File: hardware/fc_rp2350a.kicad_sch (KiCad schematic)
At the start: 49 parts, among them Q1 AP1606, Q2 AP1606, U1 TS2306A 240GF MSM 9_C2976675, U2 RP2354A, X1 XTM25012000JT00351001

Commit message: Circuit: B3 bulk caps and ESP32-C3FH4, LDO caps, BMI270 aux pins, BOOTSEL 1k, unused pads
CIRCUIT_REVIEW B3, S2, S4, S5 and decision D9; LAYOUT_REVIEW 5.3 (pure
clean-up). Values and parts from hardware/KiCad-Library/PARTS-USED.md.

- B3: the 16 +BATT bulk caps had value "C" and no part. C90-C103 (0805)
  4.7uF 50V X5R CL21A475KBQNNNE (C98192, already C18/C19); C105/C106 (1206)
  4.7uF 50V X7R TCC1206X7R475K500HT (C380366, OpenESC).
- D9/B3: U22 is ESP32-C3FH4 (C2858491, in-package flash), as its NC SPI pins
  require; its in-package-flash pads 19, 21-24 deleted per instance (20 was
  already gone). L4 MPN MLZ2012M150WT000 (TDK, SX1281 reference BOM, LCSC not
  in the catalogue); D9 MPN/manufacturer/LCSC from the catalogue.
- S2, LP5912 windows (CIN > 0.5 uF effective, COUT 0.7-10 uF): U7 COUT C28
  22uF -> 1uF CL05A105KA5NQNC; U6 COUT C27 22uF -> 4.7uF CL05A475MP5NRNC;
  U7 CIN C26 100nF -> 1uF GRM033R61A105ME44D in the existing 0201 (an 0402
  does not fit beside U7 without moving parts; ~0.5 uF effective at 4.6 V,
  so it is marginal until U7 moves to the Core in R2, decision S1).
- S4: BMI270 U8 ASDx/ASCx (pins 2/3) were on GND, which the datasheet
  forbids; now +3.3V (VDDIO), valid for the LSM6DSV16X option too.
  Schematic: the GND drop replaced by a +3.3V symbol. Core: pads 2/3 and the
  via between them re-netted, 0.15 mm In3 stub to the In3 +3.3V pour.
- S5: BOOTSEL resistor R7 10k -> 1k (0201WMF1001TEE, C270365): 10k with the
  32k minimum pull-up gave 0.79 V against VIL 0.8 V.
- LAYOUT_REVIEW 5.3, pads on no net with nothing attached: U13/U15/U17/U19
  (AT32F421) 3, 8, 9, 12, 23, 24, 26-28; U14/U16/U18/U20 (NSG2065Q) NC 5, 7,
  8, 21; U7 NC 2; U21 6 (XTB, TCXO), 9, 10 (DIO2/3); Core U2 55-59 (QSPI,
  in-package flash). 60 pads in all; U8 kept for joint symmetry. AT32
  firmware must keep the dropped pins as outputs or pulled.
- Footprint values and fields synced from the schematic for the changed refs.

Deferred: RX LED D9 to +4v5 (S10). +4v5 copper is 1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
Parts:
- R7: value 10k -> 1k; LCSC C106225 -> C270365; MPN RC0201FR-0710KL -> 0201WMF1001TEE; Manufacturer YAGEO -> UNI-ROYAL
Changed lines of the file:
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@@
 			)
 		)
-		(property "Value" "10k"
+		(property "Value" "1k"
 			(at 259.08 212.09 90)
 			(show_name no)
@@
 			)
 		)
-		(property "LCSC" "C106225"
+		(property "LCSC" "C270365"
 			(at 259.08 207.01 0)
 			(hide yes)
@@
 			)
 		)
-		(property "MPN" "RC0201FR-0710KL"
+		(property "MPN" "0201WMF1001TEE"
 			(at 71.12 46.99 0)
 			(hide yes)
@@
 			)
 		)
-		(property "Manufacturer" "YAGEO"
+		(property "Manufacturer" "UNI-ROYAL"
 			(at 71.12 46.99 0)
 			(hide yes)

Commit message: Owner rules: no component silk, pad labels and values, no wordmark text, MPN + maker on every BOM line
The owner rules adopted in PLAN.md (pcb-agent-commons, 2026-10-06), applied
where they are local edits:

- No component silkscreen. J91's reference was the only visible one (Core
  B.Silkscreen, under the LGA) and is hidden. Footprint silk graphics removed
  per instance: Base 234, Core 72. Kept: connector outlines and pin-1 marks
  (USB1, U12 SH-6, Card1, JP1) and the LGA pin-1 marks (J90, J91). Base
  lib_footprint_mismatch warnings 31 -> 40 as a result.
- Solder-pad labels: Core J53 (GND) had none, now "gnd" in the style of J52's
  label. The SH-6 per-pin labels ("10v gnd T0", "R0 gnd R1") become the port
  name "DJI" (connectors: name and pin-1 mark only). Core J48-J51 have no room:
  0.5 mm to J44 above, 0.93 mm to the board edge below. CIRCUIT_REVIEW 8.3
  moves them off the LGA in R2, so their labels go with that move.
- Pad values: all 40 solder-pad symbols said "5V". Each now carries its
  function (5V, GND, LED, BUZ+/BUZ-, 10V, 4V5, CAM, VTX, SCL, SDA, TX0/RX0,
  TX1/RX1, PIO_TX0/PIO_RX0; off-board J19 ADC2, J22 GND, J46/J47 NC).
- No "Drone" text: the "OpenDrone" wordmark on Core F.Silkscreen (9 filled
  polygons in two groups) is removed; a TODO for the incutec wordmark from the
  brand repo sits on User.Comments (not fabricated). No other such text on any
  copper, mask or silk layer of either board.
- BOM: lines missing manufacturer or MPN 41 -> 1. MPNs come from
  PARTS-USED.md by LCSC number. Manufacturers come from the catalogue symbol,
  this design's spelling for the same MPN family, or the committed datasheet
  (NSIC, Sofng, Jiangsu Changjing, Hirose). Still open: Rsense2
  ASR-S-3-0.2F (C695806), whose manufacturer nothing in the catalogue states.
  U24 (board outline) and TP9 (BOOT solder pad) are not parts: excluded from
  BOM and position files.
- 0201 default / minimal capacitance: respected in the circuit commit (C26
  stays 0201; no belt-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
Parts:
- R14: MPN (none) -> RTT012401FTH; Manufacturer (none) -> RALEC
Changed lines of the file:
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@@
 			)
 		)
-		(property "MPN" ""
+		(property "MPN" "RTT012401FTH"
 			(at 171.45 138.43 0)
 			(hide yes)
@@
 			)
 		)
-		(property "Manufacturer" ""
+		(property "Manufacturer" "RALEC"
 			(at 171.45 138.43 0)
 			(hide yes)

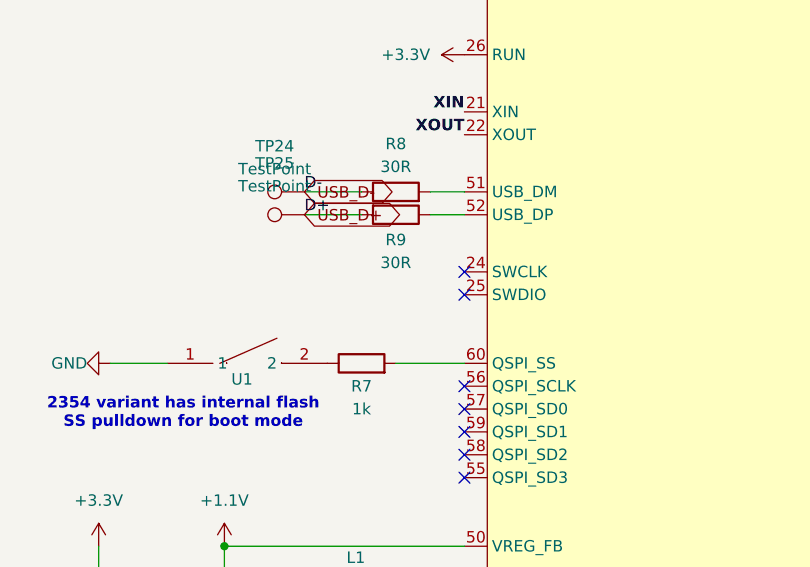
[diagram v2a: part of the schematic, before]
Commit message: Schematic: LGA nets per the R2a spec, S1/S2/B2/D7
- LGA (core_interface, generated by tools/lga_gen.py --sheet and re-saved by
  kicad-cli): J90/J91 get the 46 pins and nets of LGA_SPEC.md. 10V_ENABLE
  (B1), +3.3V (S1) and +10V (S2) no longer cross; PU0RX, SWDIO, SWCLK do.
- B2: SH-6 U12 pin 6 (DJI SBUS) leaves UART1_RX (ESP32-C3 TX) and joins
  PU0RX (RP2354A GPIO3, PIO UART0 RX); PU0RX becomes a global net so it
  crosses the LGA.
- D7: RP2354A SWCLK/SWDIO (U2.24/.25, no-connect before) go to the LGA and
  to TP32 SWCLK / TP31 SWDIO, 0.8 mm test pads on the Base (not in the BOM).
- S2: VTX pads move to the Base next to the SH-6: J41 +10V and J51 (was a
  second +10V pad on the Core) GND, on lib:SolderPad_1.2x1.2mm.
- S1: U7 LP5912-3.3 and its caps move to the Core (board assignment is by
  footprint, see the board commit). CIN C26 becomes the 0402 1 uF 25 V
  CL05A105KA5NQNC (C52923) the spec places; the 0201 was the R1 stop-gap.
- D6/R24, the green power LED, was on +3.3V on the Base, which no longer
  exists there. Instead of moving it to the Core or deleting it (spec
  section 2), R24 now takes +3V3 (TLV75533 U23, fed from the same +4v5):
  same LED, same parts, no Core space used.

ERC: 31 errors before and after, same types (bus_to_net_conflict 3,
hier_label_mismatch 1, pin_not_connected 1, pin_not_driven 16, pin_to_pin 1,
power_pin_not_driven 9). Netlist J90/J91 checked pad by pad against
lga_spec.json: 0 mismatches.

Co-Authored-By: Claude Opus 5.5 <noreply@anthropic.com>
Claude-Session: https://claude.ai/code/session_01KTp3FLjVXfXdWrkmr6af7d
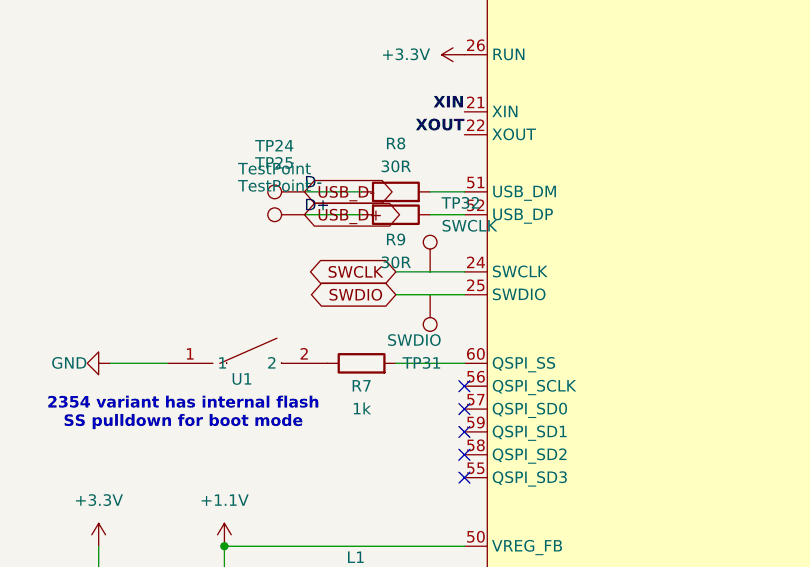
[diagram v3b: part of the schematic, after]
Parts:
- added TP31: SWDIO, lib:TestPoint_Pad_D0.8mm, symbol Connector:TestPoint
- added TP32: SWCLK, lib:TestPoint_Pad_D0.8mm, symbol Connector:TestPoint
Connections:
- net SWCLK: now reaches U2.24 (SWCLK)
- net SWCLK: now also TP32.1
- net SWDIO: now reaches U2.25 (SWDIO)
- net SWDIO: now also TP31.1
- no-connect marks 10 -> 8
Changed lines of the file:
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@@
 	)
 	(no_connect
-		(at 270.51 196.85)
-	)
-	(no_connect
 		(at 270.51 217.17)
 	)
@@
 	)
 	(no_connect
-		(at 270.51 199.39)
-	)
-	(no_connect
 		(at 270.51 209.55)
 	)
@@
 	(wire
 		(pts
+			(xy 270.51 199.39) (xy 266.7 199.39)
+		)
+		(stroke
+			(width 0)
+			(type default)
+		)
+	)
+	(wire
+		(pts
 			(xy 422.91 140.97) (xy 422.91 142.24)
 		)
@@
 	(wire
 		(pts
+			(xy 266.7 196.85) (xy 262.89 196.85)
+		)
+		(stroke
+			(width 0)
+			(type default)
+		)
+	)
+	(wire
+		(pts
 			(xy 165.1 241.3) (xy 172.72 241.3)
 		)
@@
 	(wire
 		(pts
+			(xy 270.51 196.85) (xy 266.7 196.85)
+		)
+		(stroke
+			(width 0)
+			(type default)
+		)
+	)
+	(wire
+		(pts
 			(xy 119.38 298.45) (xy 130.81 298.45)
 		)
@@
 	(wire
 		(pts
+			(xy 266.7 199.39) (xy 262.89 199.39)
+		)
+		(stroke
+			(width 0)
+			(type default)
+		)
+	)
+	(wire
+		(pts
 			(xy 134.62 278.13) (xy 134.62 269.24)
 		)
@@
 		)
 	)
+	(global_label "SWCLK"
+		(shape bidirectional)
+		(at 262.89 196.85 180)
+		(effects
+			(font
+				(size 1.27 1.27)
+			)
+			(justify right)
+		)
+		(property "Intersheetrefs" "${INTERSHEET_REFS}"
+			(at 262.89 196.85 0)
+			(hide yes)
+			(show_name no)
+			(do_not_autoplace no)
+			(effects
+				(font
+					(size 1.27 1.27)
+				)
+			)
+		)
+	)
 	(global_label "USB_D+"
 		(shape bidirectional)
@@
 		)
 	)
+	(global_label "SWDIO"
+		(shape bidirectional)
+		(at 262.89 199.39 180)
+		(effects
+			(font
+				(size 1.27 1.27)
+			)
+			(justify right)
+		)
+		(property "Intersheetrefs" "${INTERSHEET_REFS}"
+			(at 262.89 199.39 0)
+			(hide yes)
+			(show_name no)
+			(do_not_autoplace no)
+			(effects
+				(font
+					(size 1.27 1.27)
+				)
+			)
+		)
+	)
 	(hierarchical_label "GYRO_CS"
 		(shape output)
@@
 	)
 	(symbol
+		(lib_id "Connector:TestPoint")
+		(at 266.7 196.85 0)
+		(unit 1)
+		(body_style 1)
+		(exclude_from_sim no)
+		(in_bom no)
+		(on_board yes)
+		(in_pos_files no)
+		(dnp no)
+		(fields_autoplaced yes)
+		(property "Reference" "TP32"
+			(at 267.97 189.23 0)
+			(show_name no)
+			(do_not_autoplace no)
+			(effects
+				(font
+					(size 1.27 1.27)
+				)
+				(justify left)
+			)
+		)
+		(property "Value" "SWCLK"
+			(at 267.97 191.77 0)
+			(show_name no)
+			(do_not_autoplace no)
+			(effects
+				(font
+					(size 1.27 1.27)
+				)
+				(justify left)
+			)
+		)
+		(property "Footprint" "lib:TestPoint_Pad_D0.8mm"
+			(at 266.7 196.85 0)
+			(hide yes)
+			(show_name no)
+			(do_not_autoplace no)
+			(effects
+				(font
+					(size 1.27 1.27)
+				)
+			)
+		)
+		(property "Datasheet" ""
+			(at 266.7 196.85 0)
+			(hide yes)
+			(show_name no)
+			(do_not_autoplace no)
+			(effects
+				(font
+					(size 1.27 1.27)
+				)
+			)
+		)
+		(property "Description" "RP2354A SWD test pad on the Base B.Cu, through LGA pad 20"
+			(at 266.7 196.85 0)
+			(hide yes)
+			(show_name no)
+			(do_not_autoplace no)
+			(effects
+				(font
+					(size 1.27 1.27)
+				)
+			)
+		)
+		(pin "1"
+		)
+		(instances
+			(project "OpenAIO-Base"
+				(path "/fb88b6f9-ee39-4640-a9d4-04a17ceeac64/01bcb197-c5fe-4dbd-addf-fd4e1bc6a2d2"
+					(reference "TP32")
+					(unit 1)
+				)
+			)
+		)
+	)
+	(symbol
 		(lib_id "power:GND")
 		(at 149.86 139.7 0)
@@
 					(unit 1)
 				)
+			)
+		)
+	)
+	(symbol
+		(lib_id "Connector:TestPoint")
+		(at 266.7 199.39 180)
+		(unit 1)
+		(body_style 1)
+		(exclude_from_sim no)
+		(in_bom no)
+		(on_board yes)
+		(in_pos_files no)
+		(dnp no)
+		(fields_autoplaced yes)
+		(property "Reference" "TP31"
+			(at 267.97 207.01 0)
+			(show_name no)
+			(do_not_autoplace no)
+			(effects
+				(font
+					(size 1.27 1.27)
+				)
+				(justify left)
+			)
+		)
+		(property "Value" "SWDIO"
+			(at 267.97 204.47 0)
+			(show_name no)
+			(do_not_autoplace no)
+			(effects
+				(font
+					(size 1.27 1.27)
+				)
+				(justify left)
+			)
+		)
+		(property "Footprint" "lib:TestPoint_Pad_D0.8mm"
+			(at 266.7 199.39 0)
+			(hide yes)
+			(show_name no)
+			(do_not_autoplace no)
+			(effects
+				(font
+					(size 1.27 1.27)
+				)
+			)
+		)
+		(property "Datasheet" ""
+			(at 266.7 199.39 0)
+			(hide yes)
+			(show_name no)
+			(do_not_autoplace no)
+			(effects
+				(font
+					(size 1.27 1.27)
+				)
+			)
+		)
+		(property "Description" "RP2354A SWD test pad on the Base B.Cu, through LGA pad 10"
+			(at 266.7 199.39 0)
+			(hide yes)
+			(show_name no)
+			(do_not_autoplace no)
+			(effects
+				(font
+					(size 1.27 1.27)
+				)
+			)
+		)
+		(pin "1"
+		)
+		(instances
+			(project "OpenAIO-Base"
+				(path "/fb88b6f9-ee39-4640-a9d4-04a17ceeac64/01bcb197-c5fe-4dbd-addf-fd4e1bc6a2d2"
+					(reference "TP31")
+					(unit 1)
+				)

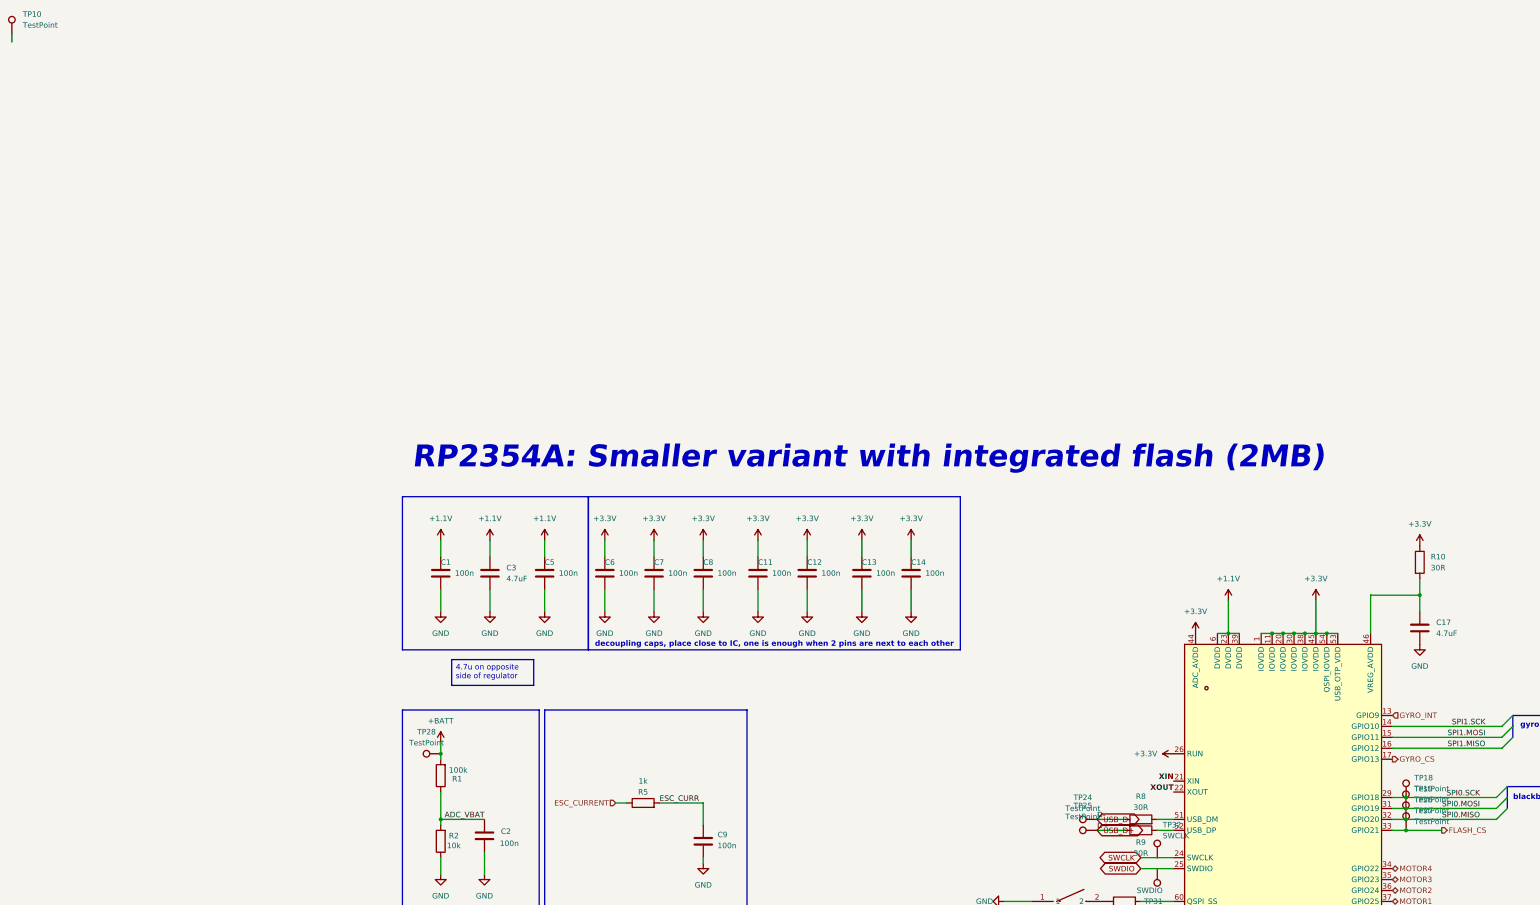
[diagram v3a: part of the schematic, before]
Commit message: Schematic readability: TP texts, C19/C107, C26, title blocks (FB5 item 6, V9-V11/M6)
- TestPoint values ('TestPoint') hidden on all sheets: the stacked TP16/TP17
  (root), TP24/TP25 and TP18/TP19/TP26/TP27 (RP2354A) texts no longer overlap.
- C19 reference/value moved left of the part (no longer printed over C107).
- C26 Description field hidden.
- Title blocks: rev r2, date 2026-10 (title added where missing) on the root,
  RP2354A, Power, IMU, OSD, Pads, ESC channel and Core interface sheets.
Edited with kicad-skip, re-saved with `kicad-cli sch upgrade --force` so the
diff stays minimal. Not done: rx_esp32c3_sx1281 and fc_blackbox title blocks
(they carry other projects' instances, OpenRX-Lite / BLACKBOX, and the headless
re-save renumbers their references); TP10 outside the frame (moving it would
detach its wire); N4 SPI0 label lift (label position is the connection point);
M7 net naming (+4v5 / +3.3V vs +3V3) left as is, it touches the LGA spec.
ERC 31 errors (unchanged).

Co-Authored-By: Claude Opus 5.5 <noreply@anthropic.com>
Claude-Session: https://claude.ai/code/session_01KTp3FLjVXfXdWrkmr6af7d
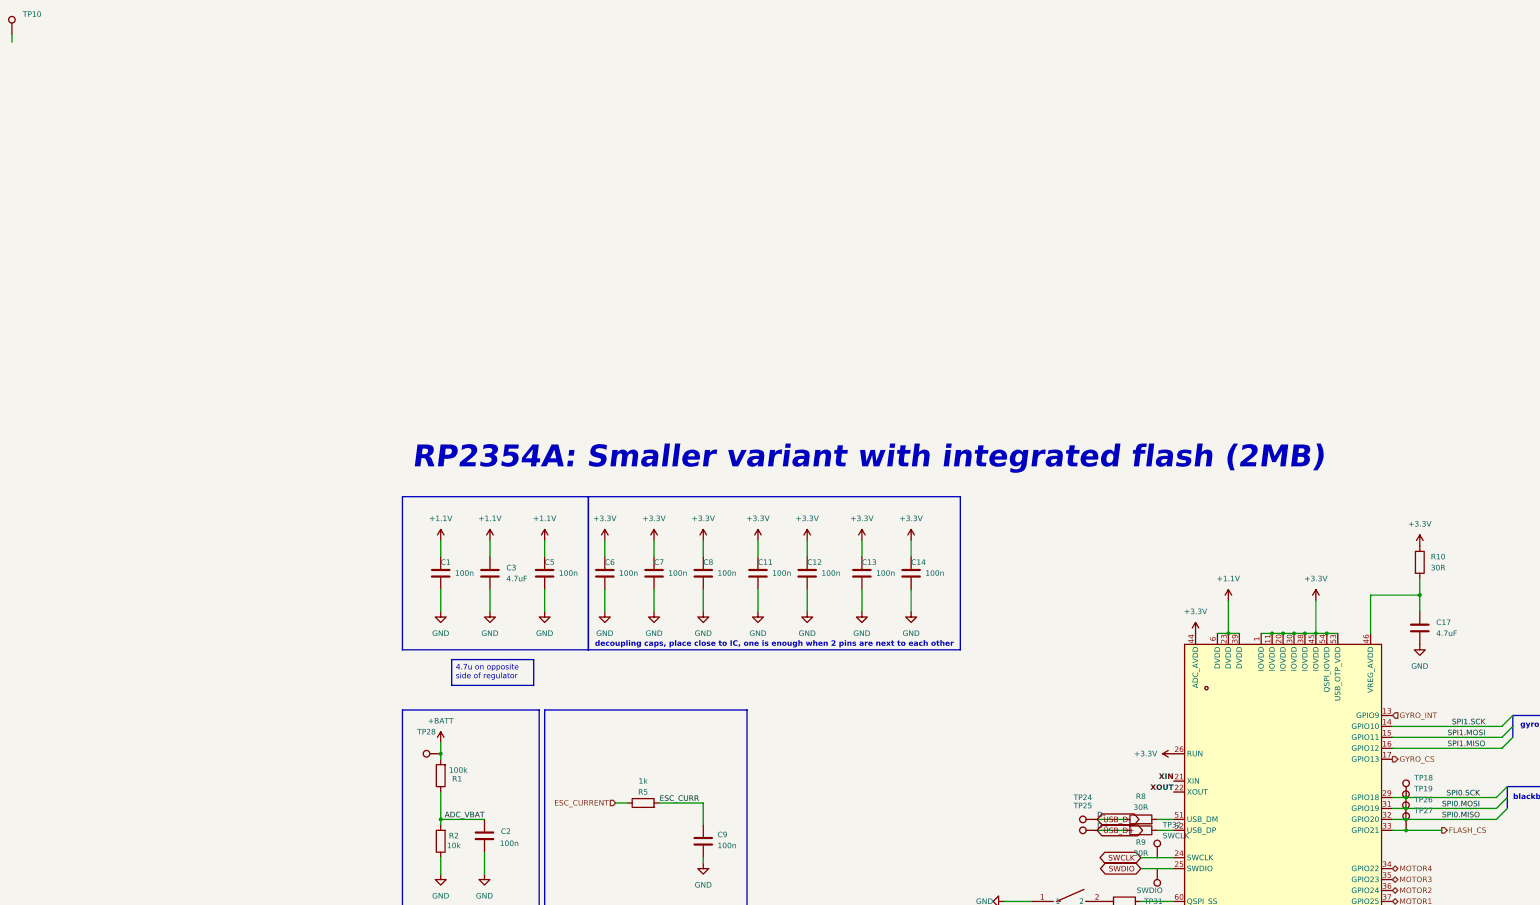
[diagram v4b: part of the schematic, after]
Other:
- title: (none) -> RP2354A flight controller
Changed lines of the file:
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@@
 	(generator_version "10.0")
 	(paper "A2")
+	(title_block
+		(title "RP2354A flight controller")
+		(date "2026-10")
+		(rev "r2")
+	)
 	(polyline
 		(pts
@@
 		(property "Value" "TestPoint"
 			(at 97.028 170.18 90)
+			(hide yes)
 			(show_name no)
 			(do_not_autoplace no)
@@
 		(property "Value" "TestPoint"
 			(at 326.39 180.8479 0)
+			(hide yes)
 			(show_name no)
 			(do_not_autoplace no)
@@
 		(property "Value" "TestPoint"
 			(at 326.39 188.4679 0)
+			(hide yes)
 			(show_name no)
 			(do_not_autoplace no)
@@
 		(property "Value" "TestPoint"
 			(at 249.428 187.325 90)
+			(hide yes)
 			(show_name no)
 			(do_not_autoplace no)
@@
 		(property "Value" "TestPoint"
 			(at 249.428 185.42 90)
+			(hide yes)
 			(show_name no)
 			(do_not_autoplace no)
@@
 		(property "Value" "TestPoint"
 			(at 326.3418 185.9279 0)
+			(hide yes)
 			(show_name no)
 			(do_not_autoplace no)
@@
 		(property "Value" "TestPoint"
 			(at 3.302 3.5616 0)
+			(hide yes)
 			(show_name no)
 			(do_not_autoplace no)
@@
 		(property "Value" "TestPoint"
 			(at 326.3418 183.3879 0)
+			(hide yes)
 			(show_name no)
 			(do_not_autoplace no)
